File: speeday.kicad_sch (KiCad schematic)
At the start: 1 part, among them U7 STM32F407VGTx

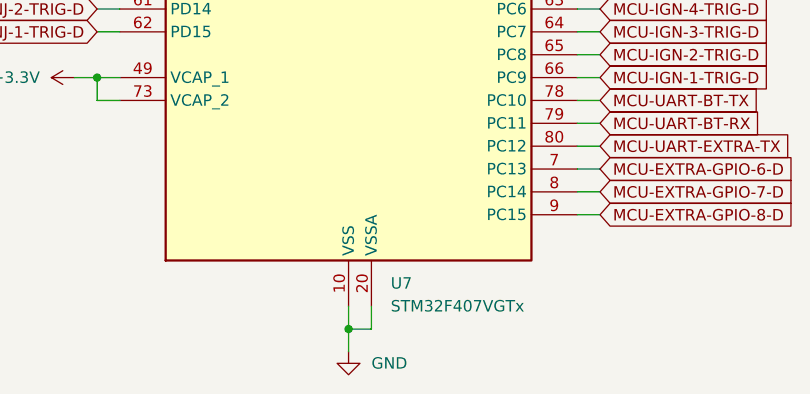
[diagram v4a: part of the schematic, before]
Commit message: Updated reference layout
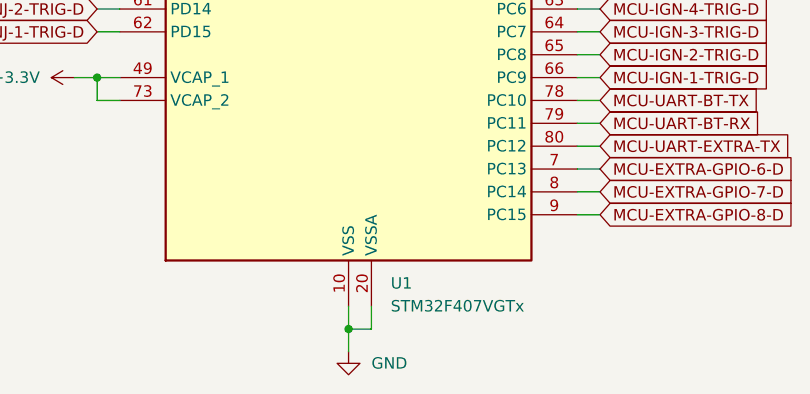
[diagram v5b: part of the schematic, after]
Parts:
- renumbered U7 to U1
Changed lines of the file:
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@@
 		(dnp no)
 		(fields_autoplaced yes)
-		(property "Reference" "#PWR035"
+		(property "Reference" "#PWR04"
 			(at 85.09 180.34 0)
 			(effects
@@
 			(project "speeday"
 				(path "/5a477c6c-8a44-40c8-a075-f8fcd765b0eb"
-					(reference "#PWR035")
+					(reference "#PWR04")
 					(unit 1)
 				)
@@
 		(dnp no)
 		(fields_autoplaced yes)
-		(property "Reference" "#PWR027"
+		(property "Reference" "#PWR01"
 			(at 58.42 143.51 0)
 			(effects
@@
 			(project "speeday"
 				(path "/5a477c6c-8a44-40c8-a075-f8fcd765b0eb"
-					(reference "#PWR027")
+					(reference "#PWR01")
 					(unit 1)
 				)
@@
 		(dnp no)
 		(fields_autoplaced yes)
-		(property "Reference" "U7"
+		(property "Reference" "U1"
 			(at 89.7733 166.37 0)
 			(effects
@@
 			(project ""
 				(path "/5a477c6c-8a44-40c8-a075-f8fcd765b0eb"
-					(reference "U7")
+					(reference "U1")
 					(unit 1)
 				)
@@
 		(dnp no)
 		(fields_autoplaced yes)
-		(property "Reference" "#PWR044"
+		(property "Reference" "#PWR05"
 			(at 93.98 21.59 0)
 			(effects
@@
 			(project ""
 				(path "/5a477c6c-8a44-40c8-a075-f8fcd765b0eb"
-					(reference "#PWR044")
+					(reference "#PWR05")
 					(unit 1)
 				)
@@
 		(dnp no)
 		(fields_autoplaced yes)
-		(property "Reference" "#PWR043"
+		(property "Reference" "#PWR02"
 			(at 60.96 44.45 0)
 			(effects
@@
 			(project ""
 				(path "/5a477c6c-8a44-40c8-a075-f8fcd765b0eb"
-					(reference "#PWR043")
+					(reference "#PWR02")
 					(unit 1)
 				)
@@
 		(dnp no)
 		(fields_autoplaced yes)
-		(property "Reference" "#PWR032"
+		(property "Reference" "#PWR03"
 			(at 78.74 21.59 0)
 			(effects
@@
 			(project "speeday"
 				(path "/5a477c6c-8a44-40c8-a075-f8fcd765b0eb"
-					(reference "#PWR032")
+					(reference "#PWR03")
 					(unit 1)
 				)

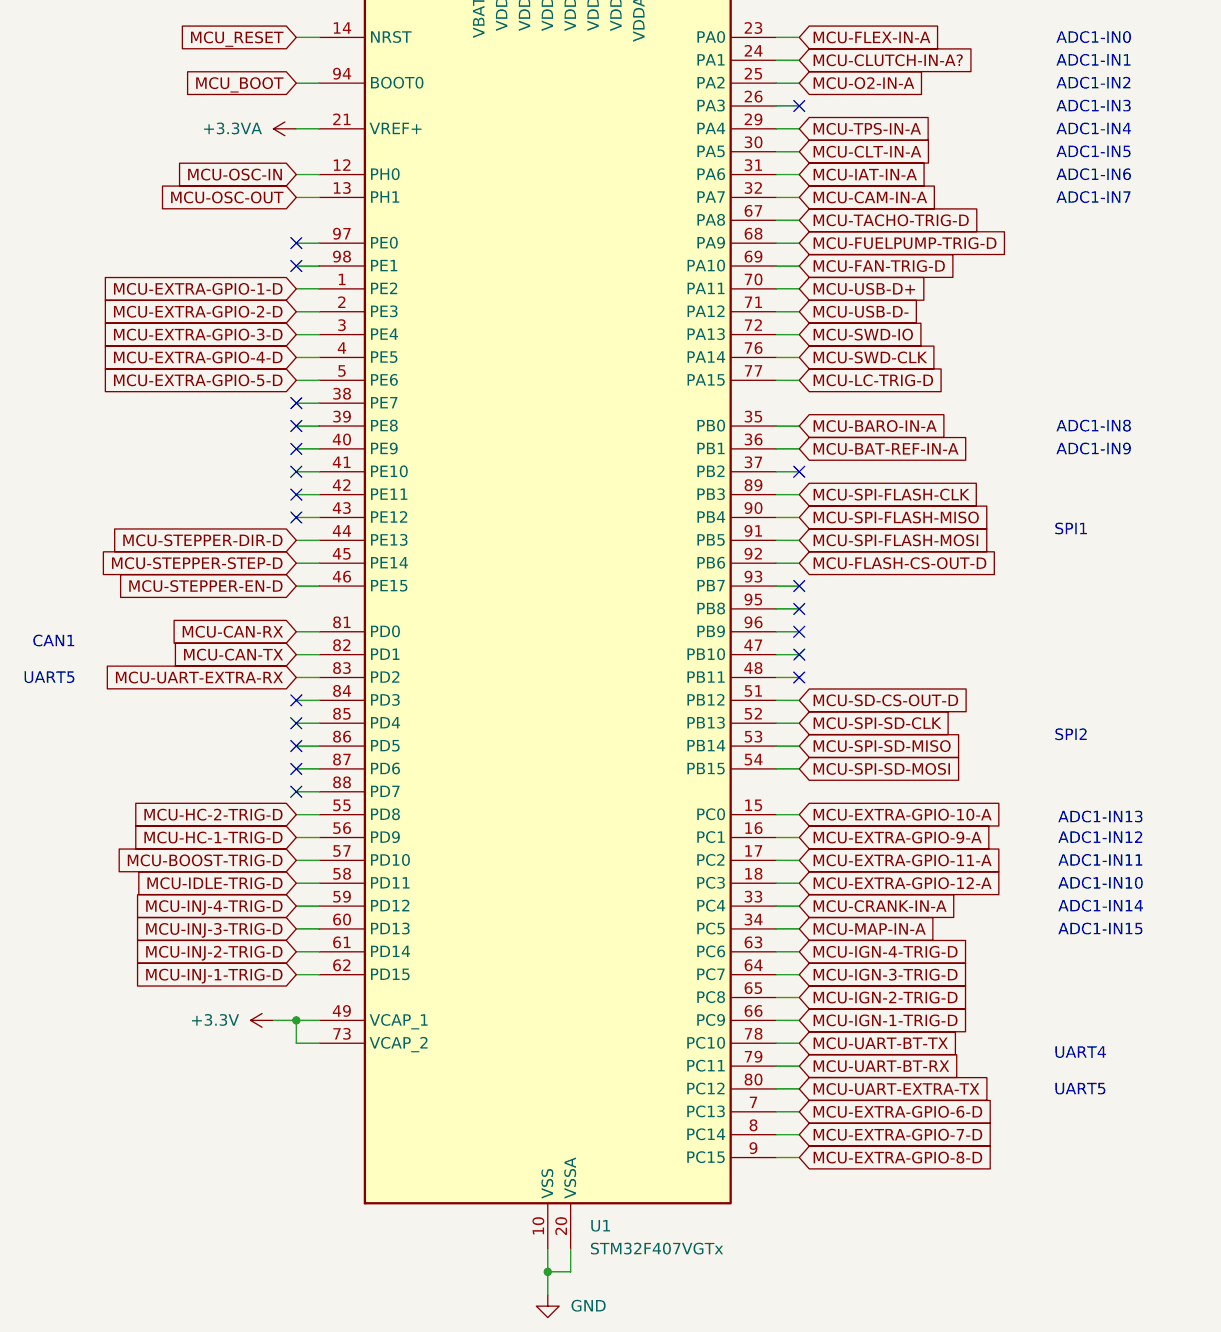
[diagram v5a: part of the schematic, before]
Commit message: Change power layout, add low frequency crystal
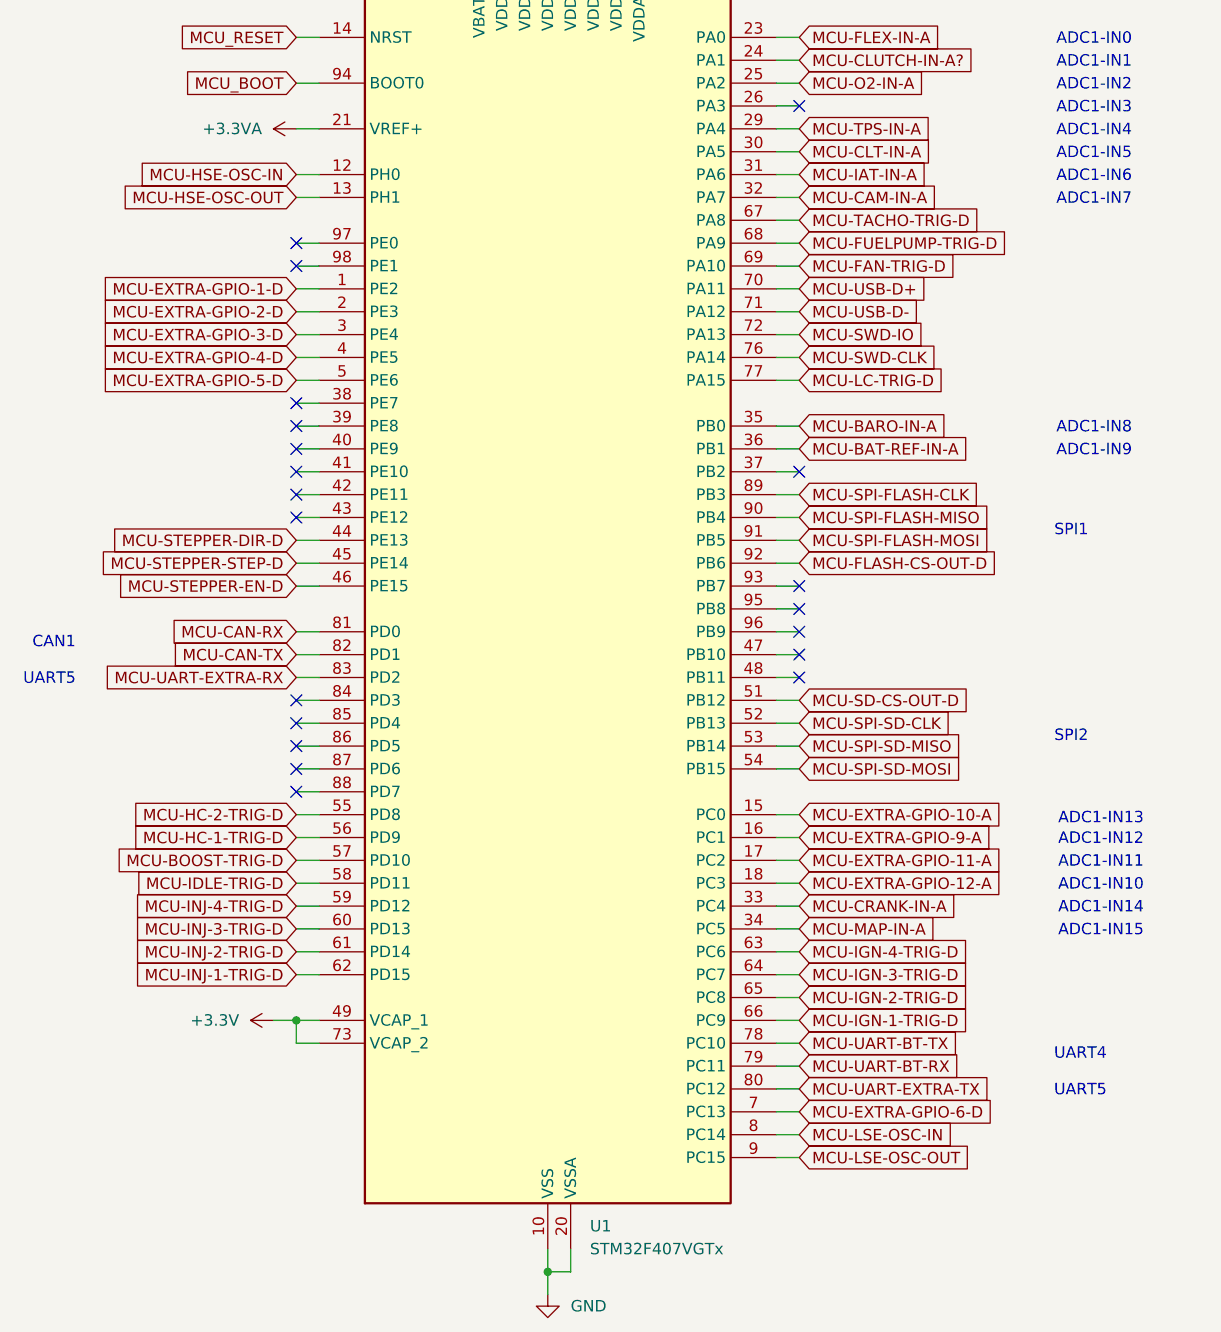
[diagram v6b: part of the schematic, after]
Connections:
- net MCU-EXTRA-GPIO-7-D renamed MCU-LSE-OSC-IN
- net MCU-EXTRA-GPIO-8-D renamed MCU-LSE-OSC-OUT
- net MCU-OSC-IN renamed MCU-HSE-OSC-IN
- net MCU-OSC-OUT renamed MCU-HSE-OSC-OUT
